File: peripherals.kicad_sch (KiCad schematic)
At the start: 8 parts, among them CN1 PJ-3059-B, J39 PZ2.54-1*9, SW2 SS-22D03-G040

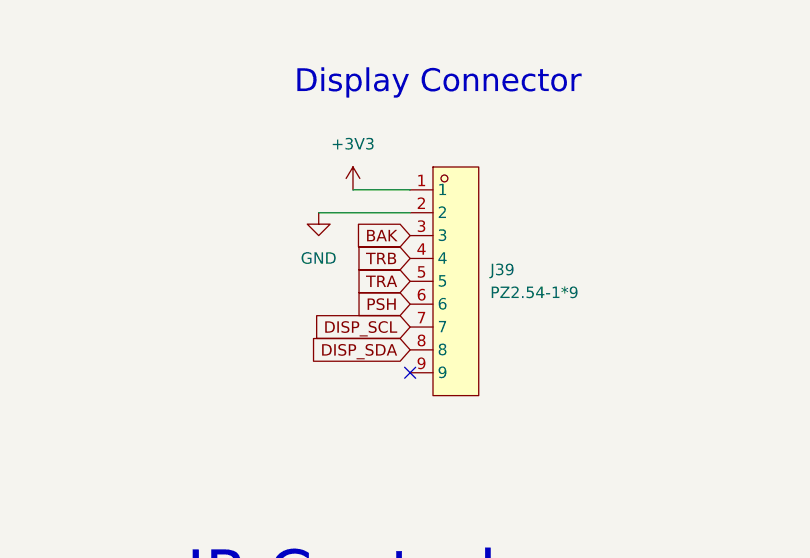
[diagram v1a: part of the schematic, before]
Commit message: Replace LVDS with RM2 Wi-Fi, add PSRAM, remove display header
- Remove the LVDS transceivers, RJ45s and their protection and termination.
  The sheet becomes wireless.kicad_sch with a Raspberry Pi RM2 (U9) on
  GPIO 32 (WL_ON), 33 (CS), 34 (DATA, via 470R and 10k as on Pico 2 W) and
  35 (CLK), reusing the routed LVDS traces.
- RM2 sits at the left edge with its antenna flush, away from the CPU and
  flash. The footprint carries the datasheet's 35.5 x 18.5 mm RF keep-out
  on every copper layer; side pads moved out 0.5 mm to match datasheet
  Figure 6. The In2 +3V3 trunk moved from x=54.15 to x=60.5 to clear it.
- Add an APS6404L 8 MB QSPI PSRAM (U10) directly under the flash, sharing
  its bus, with CS on GPIO 47 (XIP_CS1) and a 10k pull-up so it stays
  deselected while the bootrom reads flash.
- Remove the front-panel header J39 and its copper; GPIO 40, 41, 43, 45
  and 46 are now no-connects.
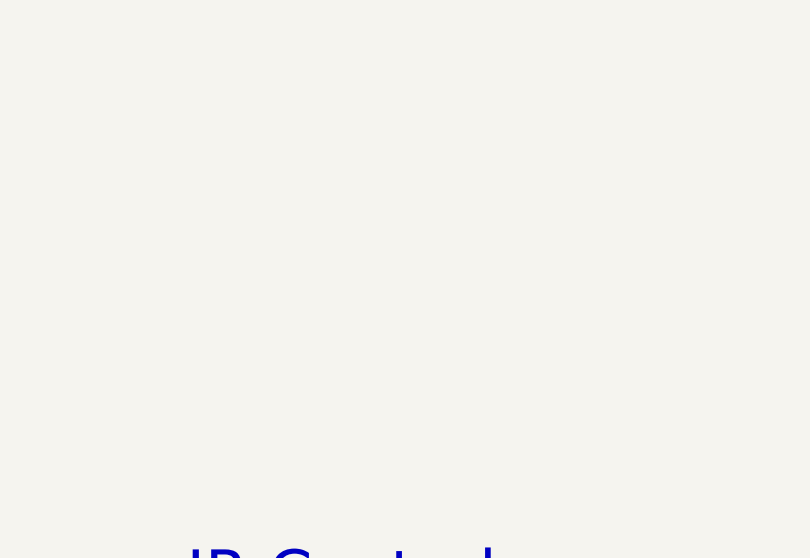
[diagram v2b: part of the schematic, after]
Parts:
- removed J39: PZ2.54-1*9, EasyEDA:HDR-TH_9P-P2.54-V-M, symbol EasyEDA:PZ2.54-1*9
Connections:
- no-connect marks 4 -> 3
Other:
- note removed: "Display Connector"

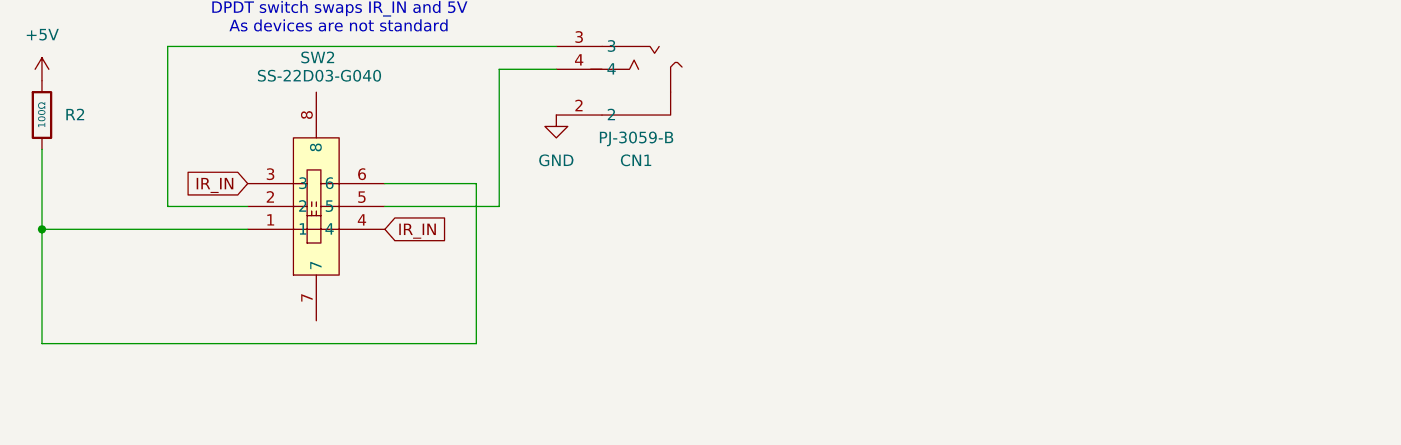
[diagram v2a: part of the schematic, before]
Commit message: Clamp IR_IN at the jack: 1k series resistor R76 and B5819W to +3V3 (D51)
SW2's IR pins become IR_RAW; GPIO42 is an ADC pin and not 5 V tolerant.
Audit item 3 marked done; README part counts updated.
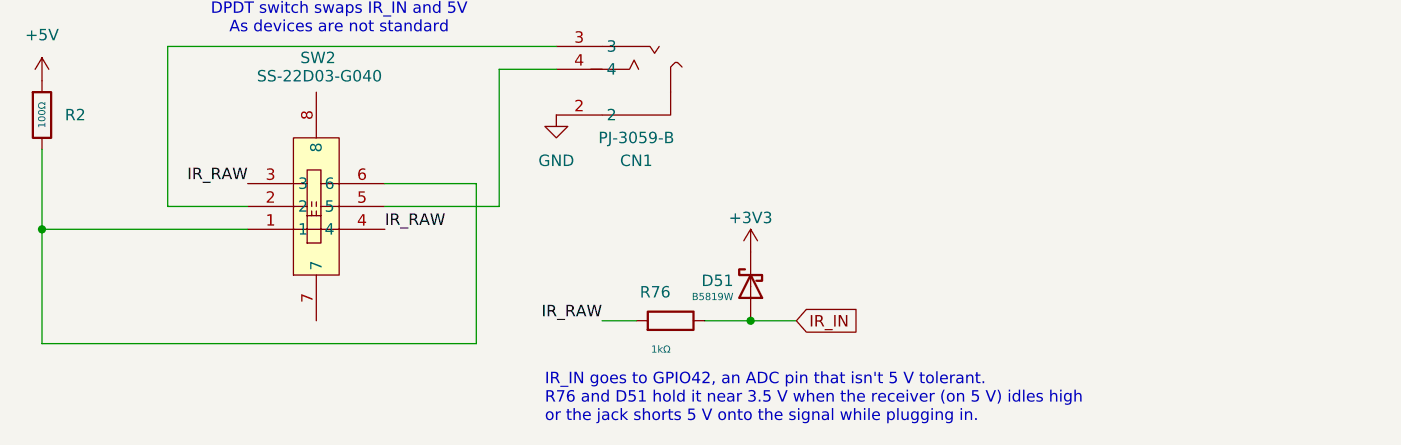
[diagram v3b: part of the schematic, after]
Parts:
- added D51: B5819W, PixelBlit:D_SOD-123, symbol PixelBlit:Schottky,B5819W
- added R76: 1kΩ, PixelBlit:R_0402, symbol PixelBlit:0402,1kΩ
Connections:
- net +3V3: now also D51.1
- net IR_IN: now also D51.2, R76.2; no longer SW2.3, SW2.4
- new net IR_RAW: R76.1, SW2.3, SW2.4
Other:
- note added: "IR_IN goes to GPIO42, an ADC pin that isn't 5 V tolerant. R76 and D51 hold it near 3.5 V when the receiver (on 5 V) idles high or the jack shorts 5 V onto the signal while plugging in."
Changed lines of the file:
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@@
-		)
-	)
-	(global_label "IR_IN"
-		(shape input)
-		(at 87.63 105.41 180)
-		(fields_autoplaced yes)
-		(effects
-			(font
-				(size 1.27 1.27)
-			)
-			(justify right)
-		)
-		(property "Intersheetrefs" "${INTERSHEET_REFS}"
-			(at 79.8671 105.41 0)
-			(hide yes)
-			(show_name no)
-			(do_not_autoplace no)
-			(effects
-				(font
-					(size 1.27 1.27)
-				)
-				(justify right)
-			)
 		)
 	)
@@
 				)
 				(justify right)
-			)
-		)
-	)
-	(global_label "IR_IN"
-		(shape input)
-		(at 102.87 110.49 0)
-		(fields_autoplaced yes)
-		(effects
-			(font
-				(size 1.27 1.27)
-			)
-			(justify left)
-		)
-		(property "Intersheetrefs" "${INTERSHEET_REFS}"
-			(at 110.6329 110.49 0)
-			(hide yes)
-			(show_name no)
-			(do_not_autoplace no)
-			(effects
-				(font
-					(size 1.27 1.27)
-				)
-				(justify left)
 			)
 		)
@@
 		)
 	)
+	(label "IR_RAW" (at 87.63 105.41 180) (fields_autoplaced yes) (effects (font (size 1.27 1.27)) (justify right bottom)))
+	(label "IR_RAW" (at 102.87 110.49 0) (fields_autoplaced yes) (effects (font (size 1.27 1.27)) (justify left bottom)))
+	(label "IR_RAW" (at 127 120.65 180) (fields_autoplaced yes) (effects (font (size 1.27 1.27)) (justify right bottom)))
+	(wire (pts (xy 127 120.65) (xy 130.81 120.65)) (stroke (width 0) (type default)))
+	(symbol (lib_id "PixelBlit:0402,1kΩ") (at 134.62 120.65 90) (unit 1) (body_style 1) (exclude_from_sim no) (in_bom yes) (on_board yes) (in_pos_files yes) (dnp no) (property "Reference" "R76" (at 134.62 117.475 90) (effects (font (size 1.27 1.27)) (justify left))) (property "Value" "1kΩ" (at 134.62 123.825 90) (effects (font (size 0.8 0.8)) (justify left))) (property "Footprint" "PixelBlit:R_0402" (at 134.62 120.65 0) (effects (font (size 1.27 1.27))) (hide yes)) (property "Datasheet" "https://www.lcsc.com/datasheet/lcsc_datasheet_2206010216_UNI-ROYAL-Uniroyal-Elec-0402WGF1001TCE_C11702.pdf" (at 134.62 120.65 0) (effects (font (size 1.27 1.27))) (hide yes)) (property "Description" "62.5mW Thick Film Resistors 50V ±100ppm/°C ±1% 1kΩ 0402 Chip Resistor - Surface Mount ROHS" (at 134.62 120.65 0) (effects (font (size 1.27 1.27))) (hide yes)) (property "LCSC" "C11702" (at 134.62 120.65 0) (effects (font (size 1.27 1.27))) (hide yes)) (property "Stock" "8973314" (at 134.62 120.65 0) (effects (font (size 1.27 1.27))) (hide yes)) (property "Price" "0.004USD" (at 134.62 120.65 0) (effects (font (size 1.27 1.27))) (hide yes)) (property "Process" "SMT" (at 134.62 120.65 0) (effects (font (size 1.27 1.27))) (hide yes)) (property "Minimum Qty" "20" (at 134.62 120.65 0) (effects (font (size 1.27 1.27))) (hide yes)) (property "Attrition Qty" "10" (at 134.62 120.65 0) (effects (font (size 1.27 1.27))) (hide yes)) (property "Class" "Basic Component" (at 134.62 120.65 0) (effects (font (size 1.27 1.27))) (hide yes)) (property "Category" "Resistors,Chip Resistor - Surface Mount" (at 134.62 120.65 0) (effects (font (size 1.27 1.27))) (hide yes)) (property "Manufacturer" "UNI-ROYAL(Uniroyal Elec)" (at 134.62 120.65 0) (effects (font (size 1.27 1.27))) (hide yes)) (property "Part" "0402WGF1001TCE" (at 134.62 120.65 0) (effects (font (size 1.27 1.27))) (hide yes)) (property "Resistance" "1kΩ" (at 134.62 120.65 0) (effects (font (size 1.27 1.27))) (hide yes)) (property "Power(Watts)" "62.5mW" (at 134.62 120.65 0) (effects (font (size 1.27 1.27))) (hide yes)) (property "Type" "Thick Film Resistors" (at 134.62 120.65 0) (effects (font (size 1.27 1.27))) (hide yes)) (property "Overload Voltage (Max)" "50V" (at 134.62 120.65 0) (effects (font (size 1.27 1.27))) (hide yes)) (property "Operating Temperature Range" "-55°C~+155°C" (at 134.62 120.65 0) (effects (font (size 1.27 1.27))) (hide yes)) (property "Tolerance" "±1%" (at 134.62 120.65 0) (effects (font (size 1.27 1.27))) (hide yes)) (property "Temperature Coefficient" "±100ppm/°C" (at 134.62 120.65 0) (effects (font (size 1.27 1.27))) (hide yes)) (pin "1") (pin "2") (instances (project "pixel_blit" (path "/046bafbc-5afd-4d51-a157-fe6ddaf6697d/40a520f0-6bc0-4995-b27d-f1f64b0d9bb8" (reference "R76") (unit 1)))))
+	(wire (pts (xy 138.43 120.65) (xy 148.59 120.65)) (stroke (width 0) (type default)))
+	(junction (at 143.51 120.65) (diameter 0) (color 0 0 0 0))
+	(symbol (lib_id "PixelBlit:Schottky,B5819W") (at 143.51 116.84 180) (unit 1) (body_style 1) (exclude_from_sim no) (in_bom yes) (on_board yes) (in_pos_files yes) (dnp no) (property "Reference" "D51" (at 141.605 116.205 0) (effects (font (size 1.27 1.27)) (justify left))) (property "Value" "B5819W" (at 141.605 117.983 0) (effects (font (size 0.8 0.8)) (justify left))) (property "Footprint" "PixelBlit:D_SOD-123" (at 143.51 116.84 0) (effects (font (size 1.27 1.27))) (hide yes)) (property "Datasheet" "https://www.lcsc.com/datasheet/lcsc_datasheet_2407291648_MDD-Microdiode-Semiconductor-B5819W_C64885.pdf" (at 143.51 116.84 0) (effects (font (size 1.27 1.27))) (hide yes)) (property "Description" "40V Independent Type 900mV@3A 1A SOD-123 Schottky Diodes ROHS" (at 143.51 116.84 0) (effects (font (size 1.27 1.27))) (hide yes)) (property "LCSC" "C64885" (at 143.51 116.84 0) (effects (font (size 1.27 1.27))) (hide yes)) (property "Stock" "396308" (at 143.51 116.84 0) (effects (font (size 1.27 1.27))) (hide yes)) (property "Price" "0.019USD" (at 143.51 116.84 0) (effects (font (size 1.27 1.27))) (hide yes)) (property "Process" "SMT" (at 143.51 116.84 0) (effects (font (size 1.27 1.27))) (hide yes)) (property "Minimum Qty" "15" (at 143.51 116.84 0) (effects (font (size 1.27 1.27))) (hide yes)) (property "Attrition Qty" "10" (at 143.51 116.84 0) (effects (font (size 1.27 1.27))) (hide yes)) (property "Class" "Preferred Component" (at 143.51 116.84 0) (effects (font (size 1.27 1.27))) (hide yes)) (property "Category" "Diodes,Schottky Barrier Diodes (SBD)" (at 143.51 116.84 0) (effects (font (size 1.27 1.27))) (hide yes)) (property "Manufacturer" "MDD（Microdiode Electronics）" (at 143.51 116.84 0) (effects (font (size 1.27 1.27))) (hide yes)) (property "Part" "B5819W" (at 143.51 116.84 0) (effects (font (size 1.27 1.27))) (hide yes)) (property "Rectified Current" "1A" (at 143.51 116.84 0) (effects (font (size 1.27 1.27))) (hide yes)) (property "Forward Voltage (Vf@If)" "900mV@3A" (at 143.51 116.84 0) (effects (font (size 1.27 1.27))) (hide yes)) (property "Reverse Voltage (Vr)" "40V" (at 143.51 116.84 0) (effects (font (size 1.27 1.27))) (hide yes)) (property "Diode Configuration" "Independent Type" (at 143.51 116.84 0) (effects (font (size 1.27 1.27))) (hide yes)) (property "Reverse Leakage Current (Ir)" "1mA@40V" (at 143.51 116.84 0) (effects (font (size 1.27 1.27))) (hide yes)) (pin "1") (pin "2") (instances (project "pixel_blit" (path "/046bafbc-5afd-4d51-a157-fe6ddaf6697d/40a520f0-6bc0-4995-b27d-f1f64b0d9bb8" (reference "D51") (unit 1)))))
+	(symbol (lib_id "PixelBlit:+3V3") (at 143.51 113.03 0) (unit 1) (body_style 1) (exclude_from_sim no) (in_bom yes) (on_board yes) (in_pos_files yes) (dnp no) (property "Reference" "#PWR0900" (at 146.05 111.76 0) (effects (font (size 1.27 1.27))) (hide yes)) (property "Value" "+3V3" (at 143.51 109.22 0) (effects (font (size 1.27 1.27)))) (property "Footprint" "" (at 143.51 113.03 0) (effects (font (size 1.27 1.27))) (hide yes)) (property "Datasheet" "" (at 143.51 113.03 0) (effects (font (size 1.27 1.27))) (hide yes)) (property "Description" "Power symbol creates a global label with name \"+3V3\"" (at 143.51 113.03 0) (effects (font (size 1.27 1.27))) (hide yes)) (property "ki_keywords" "global power" (at 143.51 113.03 0) (effects (font (size 1.27 1.27))) (hide yes)) (pin "1") (instances (project "pixel_blit" (path "/046bafbc-5afd-4d51-a157-fe6ddaf6697d/40a520f0-6bc0-4995-b27d-f1f64b0d9bb8" (reference "#PWR0900") (unit 1)))))
+	(global_label "IR_IN" (shape input) (at 148.59 120.65 0) (fields_autoplaced yes) (effects (font (size 1.27 1.27)) (justify left)) (property "Intersheetrefs" "${INTERSHEET_REFS}" (at 148.59 120.65 0) (effects (font (size 1.27 1.27))) (hide yes)))
+	(text "IR_IN goes to GPIO42, an ADC pin that isn't 5 V tolerant.\nR76 and D51 hold it near 3.5 V when the receiver (on 5 V) idles high\nor the jack shorts 5 V onto the signal while plugging in." (exclude_from_sim no) (at 120.65 132.08 0) (effects (font (size 1.27 1.27)) (justify left bottom)))
 )
